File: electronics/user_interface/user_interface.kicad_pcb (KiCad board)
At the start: 2 copper layers, 80 x 80 mm, 87 parts, among them J1 Conn_01x06, J2 Conn_02x05_Odd_Even, SW1 ALPS_EC11E18244A5, U1 PCF8574, U2 PCF8574

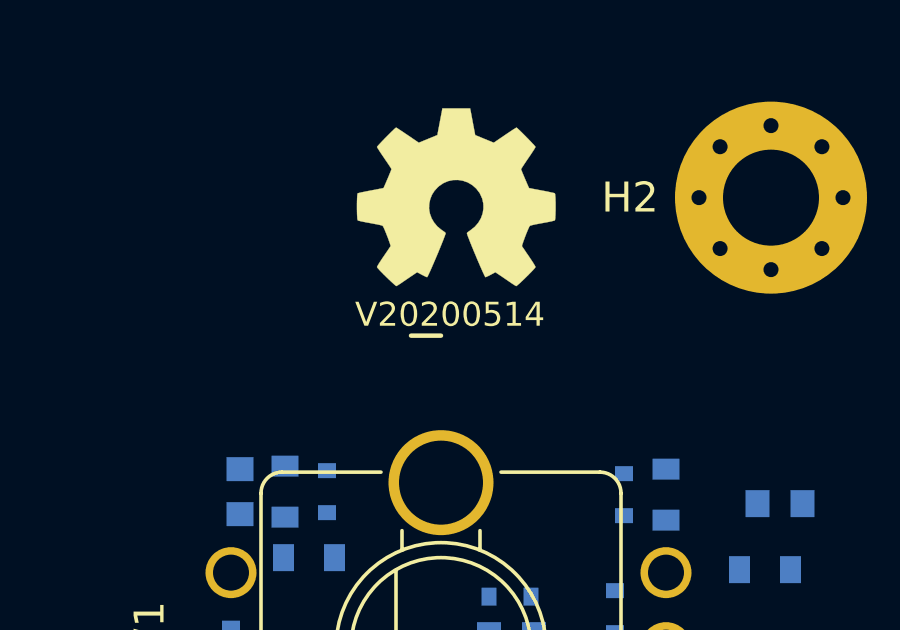
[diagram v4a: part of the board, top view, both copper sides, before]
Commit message: updated footprints to include 3dmodel of SOD-523 diode
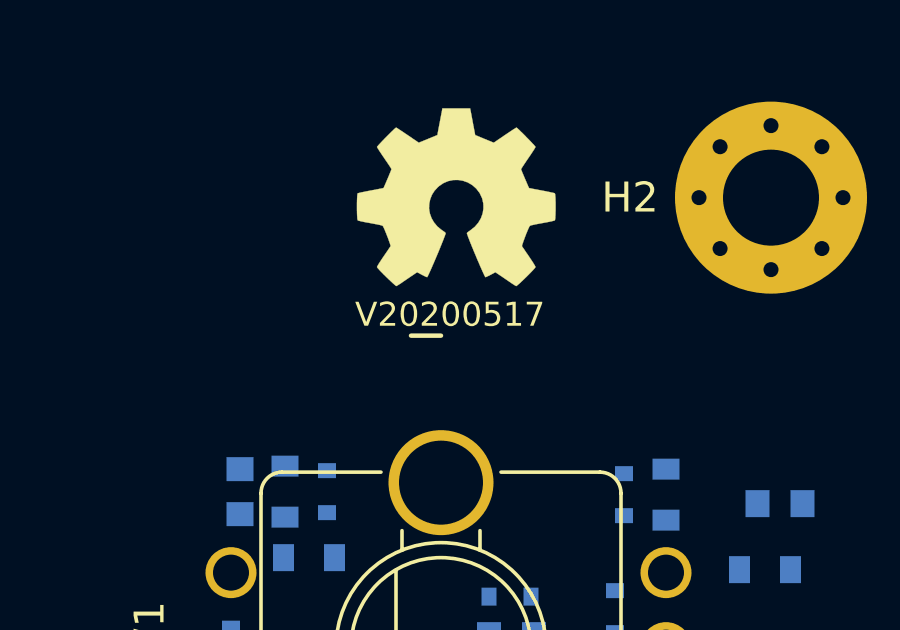
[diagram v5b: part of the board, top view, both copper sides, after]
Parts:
- N2: value V20200514 -> V20200517

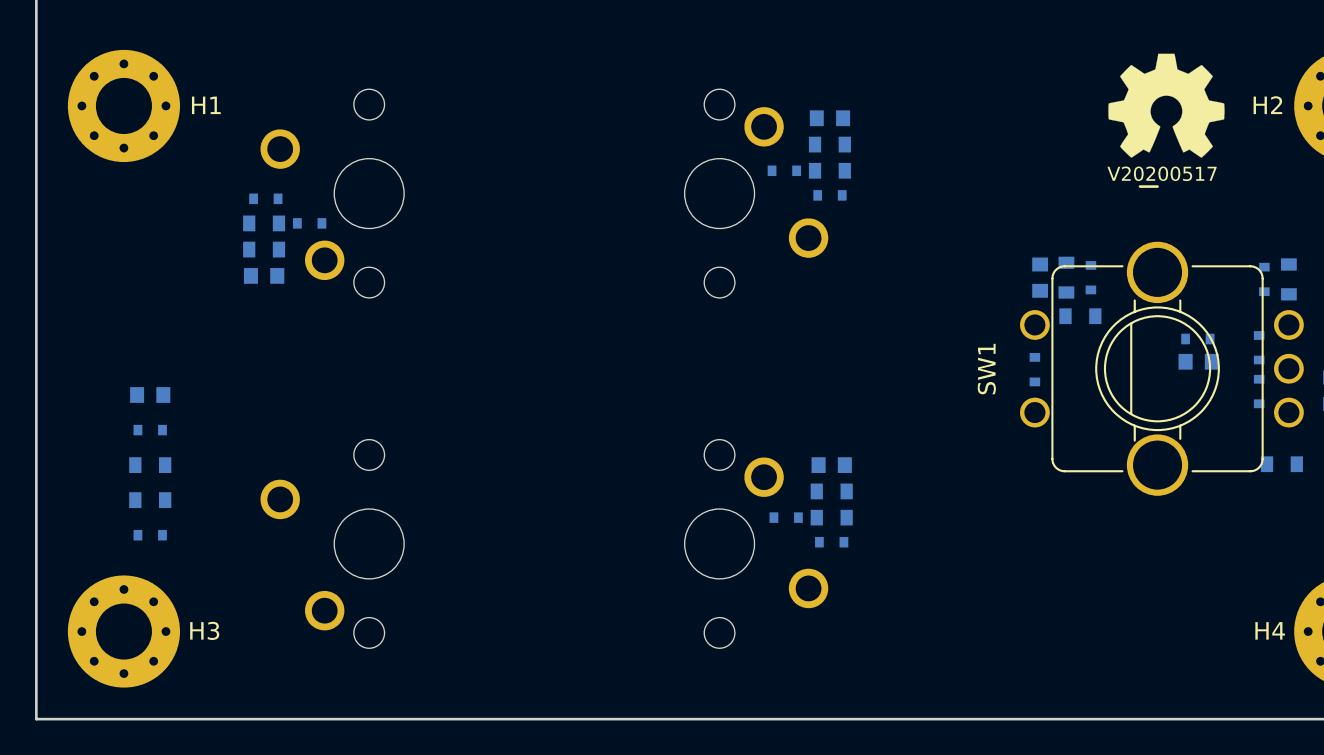
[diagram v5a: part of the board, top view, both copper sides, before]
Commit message: WIP routing of filtering on the buttons
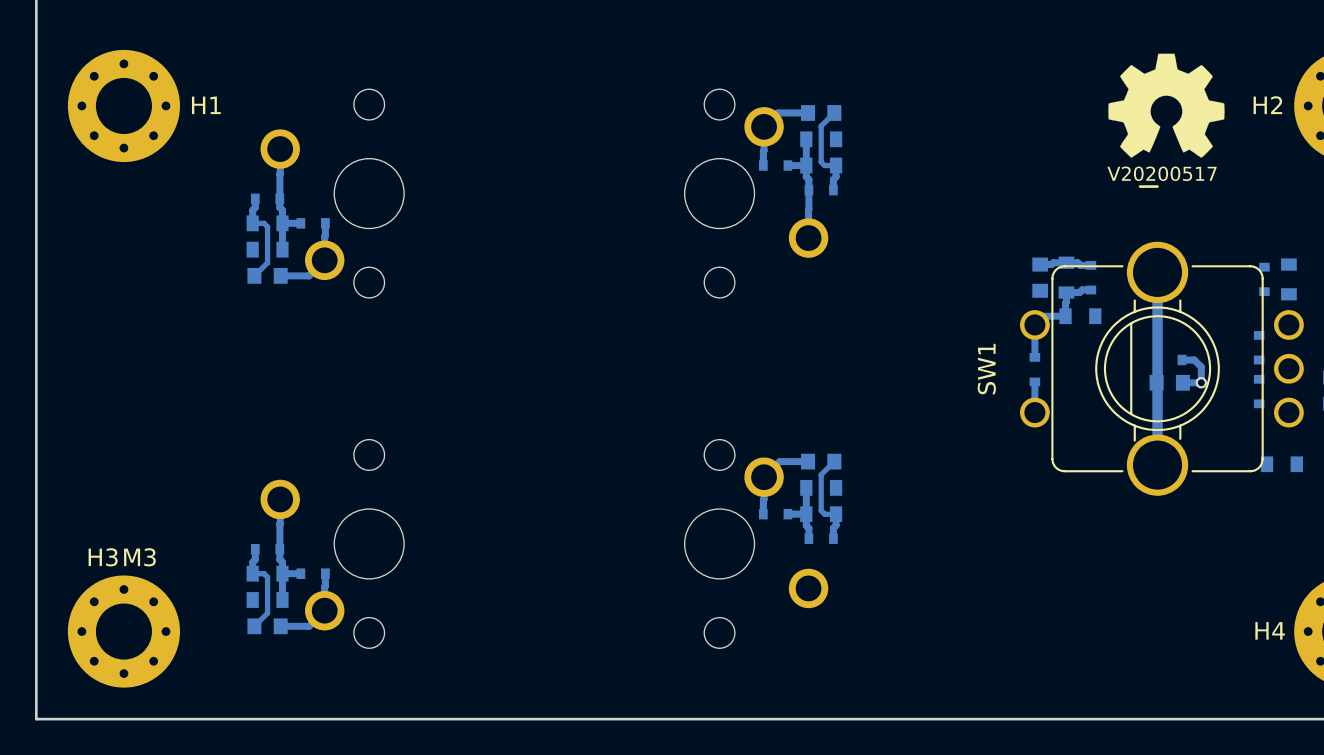
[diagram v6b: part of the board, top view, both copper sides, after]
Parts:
- moved C5 14.8 mm to (123.2, 144.7)
- moved D6 9.56 mm to (125.8, 141.7), turned to 0 degrees
- moved D2 9.55 mm to (123.2, 140.3)
- moved R16 9.13 mm to (123.2, 141.7)
- moved R13 8.80 mm to (123.2, 143.2)
- moved C11 2.04 mm to (174.7, 130.8)
- moved D15 2.00 mm to (174.7, 129.5)
- moved D8 0.63 mm to (152.2, 138.3)
- moved D4 0.63 mm to (154.8, 139.7)
- moved C7 0.63 mm to (154.8, 135.3)
- moved R15 0.63 mm to (154.8, 136.8)
- moved R18 0.63 mm to (154.8, 138.3)
- moved C6 0.58 mm to (154.8, 115.4)
- moved D3 0.58 mm to (154.8, 119.8)
- moved D7 0.58 mm to (152.2, 118.4)
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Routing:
- net /VSS: track 0.00 -> 25.0 mm, vias 0 -> 1
- net /Rotary_shield: track 0.00 -> 11.0 mm
- net Net-(D1-Pad2): track 0.00 -> 6.86 mm
- net Net-(D2-Pad2): track 0.00 -> 6.86 mm
- net Net-(D3-Pad2): track 0.00 -> 6.76 mm
- net /Rotary_push: track 0.00 -> 6.64 mm
- net /Button_00: track 0.00 -> 5.51 mm
- net /Button_02: track 0.00 -> 5.51 mm
- net /Button_01: track 0.00 -> 5.51 mm
- net /Button_03: track 0.00 -> 5.51 mm
- net Net-(D4-Pad2): track 0.00 -> 4.01 mm
- net /Rotary_push_filtered: track 0.00 -> 3.00 mm

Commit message: WIP switch filtering placement and routing, silk changes
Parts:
- moved D13 7.06 mm to (178.2, 135.6), turned to 90 degrees
- moved R20 6.91 mm to (178.9, 133.3), turned to 180 degrees
- moved R21 5.94 mm to (178.9, 126.7), turned to 180 degrees
- moved C9 5.17 mm to (181.1, 135.6)
- moved C10 4.28 mm to (181.1, 124.4), turned to 270 degrees
- moved D14 1.96 mm to (178.2, 124.4)
- moved R24 1.96 mm to (179.6, 124.4)
- moved R23 1.51 mm to (179.6, 135.6), turned to 90 degrees
- moved C8 0.30 mm to (167.3, 124.5)
- moved D12 0.30 mm to (170.2, 124.5)
- moved R19 0.30 mm to (169.6, 126.7)
- moved R22 0.30 mm to (168.8, 124.5)
- moved D11 0.20 mm to (179.8, 128.6)
- moved D10 0.10 mm to (179.8, 131.4)
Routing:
- net /VSS: track 25.0 -> 31.8 mm, vias 1 -> 4
- net /Rotary_A: track 0.00 -> 6.06 mm
- net /Rotary_B: track 0.00 -> 6.06 mm
- net /Rotary_B_filtered: track 0.00 -> 3.00 mm
- net /Rotary_A_filtered: track 0.00 -> 3.00 mm
- net Net-(D4-Pad2): track 4.01 -> 6.86 mm
- net /Rotary_push: track 6.64 -> 7.14 mm

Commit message: updated versionnumber
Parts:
- N1: footprint Symbols:OSHW-Symbol_6.7x6mm_SilkScreen -> Symbol:OSHW-Symbol_6.7x6mm_SilkScreen
- N2: value V20200517 -> V20200521
